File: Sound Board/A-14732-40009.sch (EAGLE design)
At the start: 234 parts, among them P2 AUX IN, P3 AUX OUT, P4 ORKIN R/W, P5 VOLUME, P6 0.156", P7 0.156", Q1 MPS3646, U1 OKI6295, U10 26LS32A, U11 26LS31, U12 27C040-150, U13 27C040-150, U14 YAMAHA 2151, U15 TIL7524, U16 74LS374, U17 74LS174, U18 16L8, U19 74LS11, U2 2064, U20 74LS139, U21 74LS14, U22 74LS74, U23 74LS74, U24 26LS31, U25 26LS32A, U26 74LS04, U28 YAMAHA 3012, U29 LM324D, U3 27C040, U30 MC3340, U31 HA3116, U32 TL084D, U33 TL084D, U4 6809E, U5 74LS374DW, U6 26LS32A, U7 26LS31, U8 74LS138, U9 74LS74, Y1 3.5749MHz, Y2 8MHz

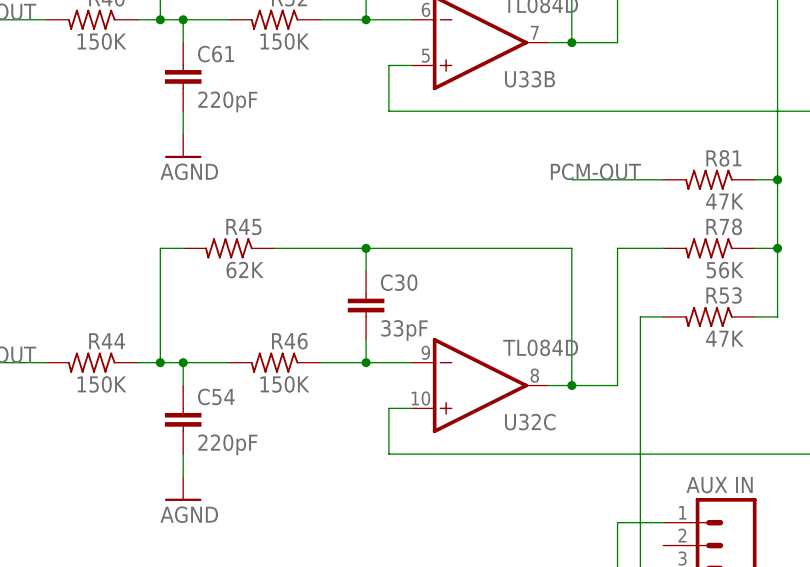
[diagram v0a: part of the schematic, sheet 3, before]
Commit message: corrected C30 to C59
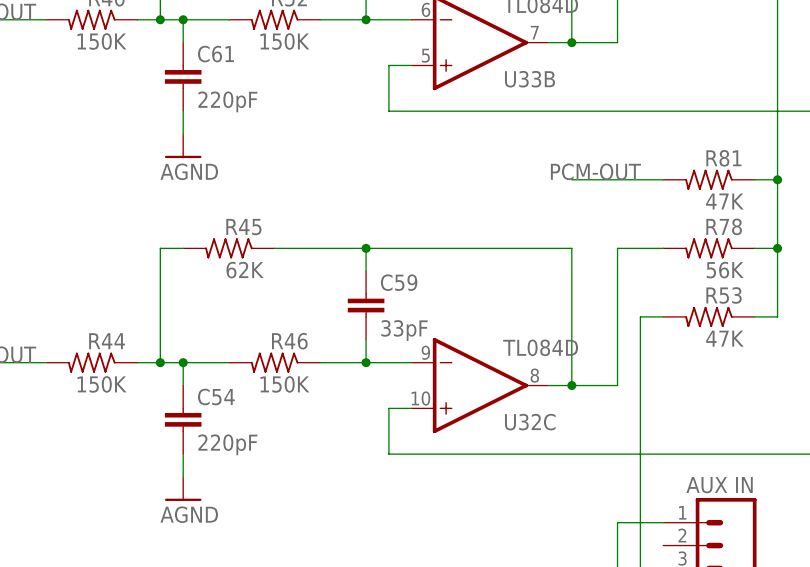
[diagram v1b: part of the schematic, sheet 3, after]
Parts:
- renumbered C30 to C59
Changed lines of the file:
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@@
 <part name="U$21" library="SparkFun-Aesthetics" deviceset="AGND" device=""/>
 <part name="R45" library="resistor" deviceset="R-US_" device="R1206" value="62K"/>
-<part name="C30" library="SparkFun-Capacitors" deviceset="1.0UF50V10%(1206)" device="" value="33pF">
+<part name="C59" library="SparkFun-Capacitors" deviceset="1.0UF50V10%(1206)" device="" value="33pF">
 <attribute name="VOLTAGE" value="50V"/>
 </part>
@@
 <instance part="U$21" gate="G$1" x="50.8" y="114.3"/>
 <instance part="R45" gate="G$1" x="55.88" y="142.24" rot="MR0"/>
-<instance part="C30" gate="G$1" x="71.12" y="134.62"/>
+<instance part="C59" gate="G$1" x="71.12" y="134.62"/>
 <instance part="R78" gate="G$1" x="109.22" y="142.24" rot="MR0"/>
 <instance part="R81" gate="G$1" x="109.22" y="149.86" rot="MR0"/>
@@
 <segment>
 <pinref part="R45" gate="G$1" pin="1"/>
-<pinref part="C30" gate="G$1" pin="1"/>
+<pinref part="C59" gate="G$1" pin="1"/>
 <wire x1="60.96" y1="142.24" x2="71.12" y2="142.24" width="0.1524" layer="91"/>
 <wire x1="71.12" y1="142.24" x2="71.12" y2="139.7" width="0.1524" layer="91"/>
@@
 <segment>
 <pinref part="R46" gate="G$1" pin="1"/>
-<pinref part="C30" gate="G$1" pin="2"/>
+<pinref part="C59" gate="G$1" pin="2"/>
 <wire x1="71.12" y1="129.54" x2="76.2" y2="129.54" width="0.1524" layer="91"/>
 <wire x1="71.12" y1="132.08" x2="71.12" y2="129.54" width="0.1524" layer="91"/>
